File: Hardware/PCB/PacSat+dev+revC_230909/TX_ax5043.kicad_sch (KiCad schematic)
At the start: 33 parts, among them P101 U_FL, U156 AX5043, U89 TPS22917DBV

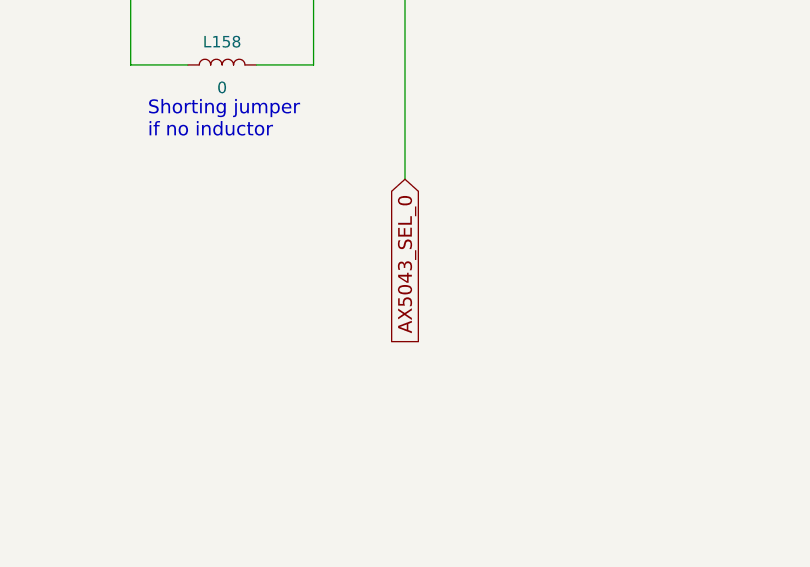
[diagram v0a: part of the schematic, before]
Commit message: Changed schematic to add Select lines for each AX5043 on the CPU.
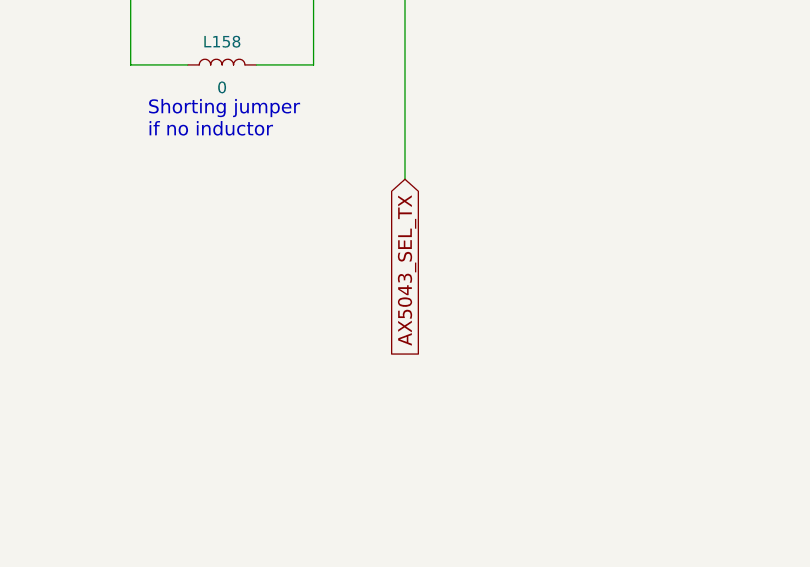
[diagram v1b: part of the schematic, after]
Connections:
- net AX5043_SEL_0 renamed AX5043_SEL_TX
